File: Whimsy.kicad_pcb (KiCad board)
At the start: 2 copper layers, 261.9 x 81 mm, 102 parts, among them J1 OLED, J2 LED Breakout, K1 KEYSW, K10 KEYSW, K11 KEYSW, K12 KEYSW, K13 KEYSW, K14 KEYSW, K15 KEYSW, K16 KEYSW, K17 KEYSW, K18 KEYSW, K19 KEYSW, K2 KEYSW, K20 KEYSW, K21 KEYSW, K22 KEYSW, K23 KEYSW, K24 KEYSW, K25 KEYSW, K26 KEYSW, K27 KEYSW, K28 KEYSW, K29 KEYSW, K3 KEYSW, K30 KEYSW, K31 KEYSW, K32 KEYSW, K33 KEYSW, K34 KEYSW, K35 KEYSW, K36 KEYSW, K37 KEYSW, K38 KEYSW, K39 KEYSW, K4 KEYSW, K40 KEYSW, K41 KEYSW, K42 KEYSW, K43 KEYSW, K44 KEYSW, K45 KEYSW, K46 KEYSW, K47 KEYSW, K5 KEYSW, K6 KEYSW, K7 KEYSW, K8 KEYSW, K9 KEYSW, SW1 Rotary_Encoder_Switch, U1 Elite-C

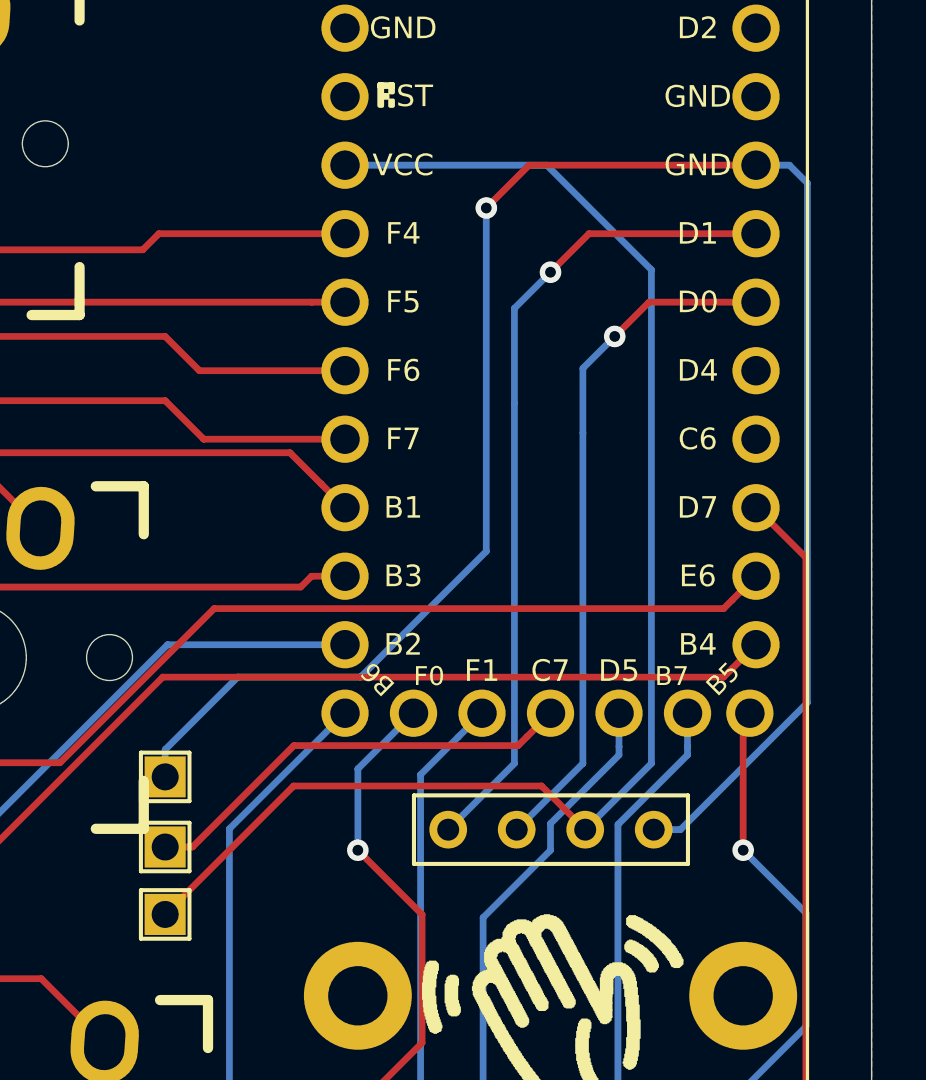
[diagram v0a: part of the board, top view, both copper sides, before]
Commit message: fixed gnd net
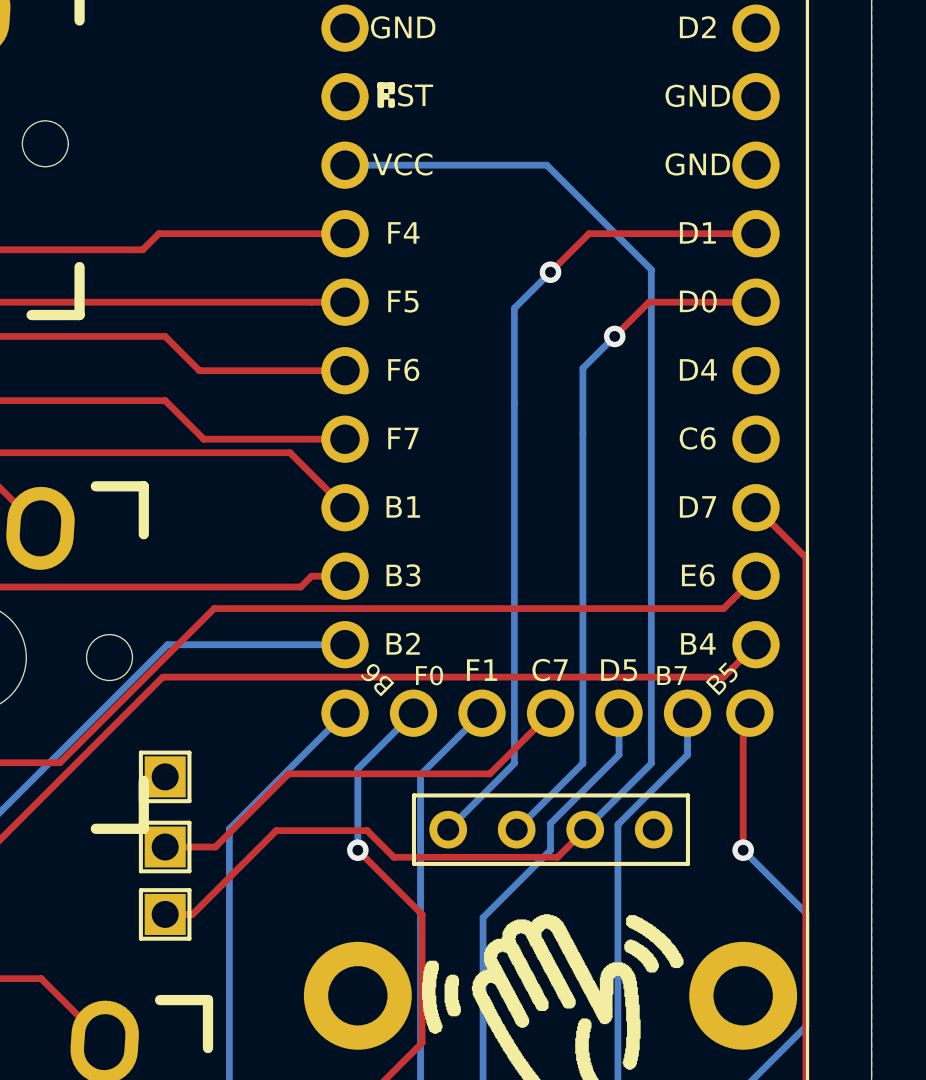
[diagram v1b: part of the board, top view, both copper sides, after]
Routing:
- net GND: track 68.4 -> 0.00 mm, vias 1 -> 0
- net VCC: track 53.0 -> 52.4 mm
- added copper zone on F.Cu, net GND
- removed copper zone on F.Cu, net (none)
